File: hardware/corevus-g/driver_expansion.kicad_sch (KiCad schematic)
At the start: 22 parts, among them T1 V_{SA}, T10 TestPoint, T11 TestPoint, T12 TestPoint, T13 TestPoint, T14 TestPoint, T15 TestPoint, T16 TestPoint, T2 SClk, T3 Gnd, T4 MOSI, T5 MISO, T6 V_{CC}IO, T7 TestPoint, T8 TestPoint, T9 TestPoint

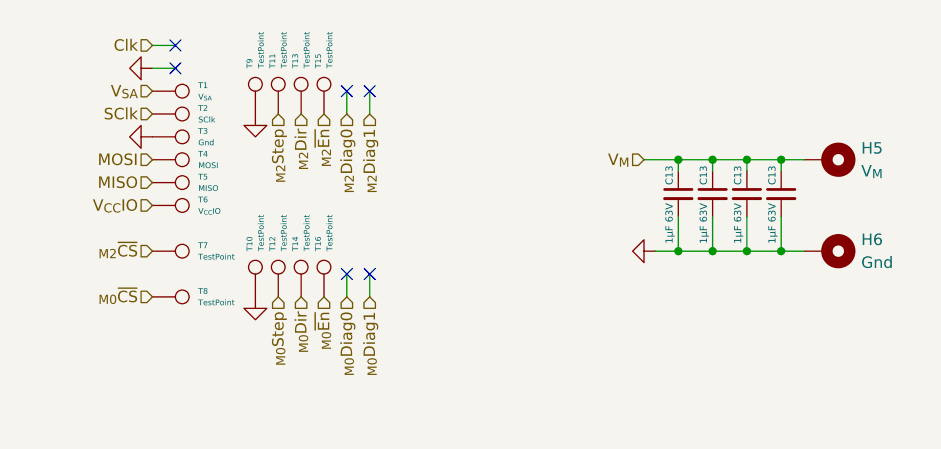
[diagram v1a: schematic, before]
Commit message: version control appears to have magically disappeared the single and dual 2160 driver files :(((((((((, but got some work done on CvG nonetheless
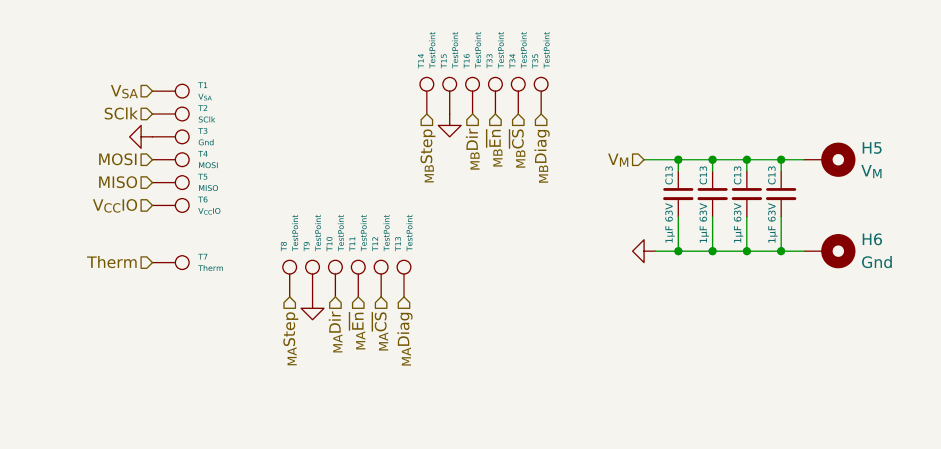
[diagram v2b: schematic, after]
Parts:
- added T13, T35: TestPoint, corevus:LGA_Spring, symbol Connector:TestPoint
- added T7: Therm, corevus:LGA_Spring, symbol Connector:TestPoint
- renumbered T14 to T10, T16 to T11, T7 to T12, T11 to T14, T9 to T15, T13 to T16, T15 to T33, T8 to T34, T12 to T8, T10 to T9
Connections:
- net _{M0}Dir renamed _{MA}Dir
- net _{M0}Step renamed _{MA}Step
- net _{M0}~{CS} renamed _{MB}~{CS}
- net _{M0}~{En} renamed _{MA}~{En}
- net _{M2}Dir renamed _{MB}Dir
- net _{M2}Step renamed _{MB}Step
- net _{M2}~{CS} renamed _{MA}~{CS}
- net _{M2}~{En} renamed _{MB}~{En}
- new net Therm: T7.1
- new net _{MA}Diag: T13.1
- new net _{MB}Diag: T35.1
- no-connect marks 6 -> 0
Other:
- moved on the sheet: T10, T11, T12, T14, T15, T16, T33, T34, T8, T9

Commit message: v0.4 mostly complete, board needs minor revisions (e.g. pin swap)
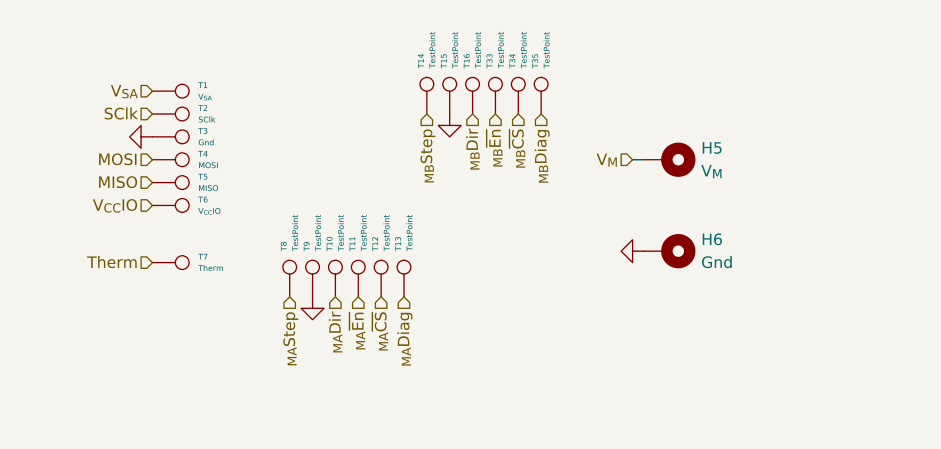
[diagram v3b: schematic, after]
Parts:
- removed C13 (x4): 1μF 63V, Capacitor_SMD:C_1206_3216Metric, symbol Device:C_Small
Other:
- moved on the sheet: H5, H6
